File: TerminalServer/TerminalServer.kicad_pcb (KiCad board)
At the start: 2 copper layers, 132 x 72 mm, 87 parts, among them J1 RJ45_LED, J2 RJ45_LED, J3 RJ45_LED, J4 RJ45_LED, J5 RJ45_LED, J6 RJ45_LED, J7 USB_C_Receptacle_USB2.0_14P, U1 PIC32MX795F512L-80x-PT, U2 XR32330EBERTR-F, U3 XR32330EBERTR-F, U4 XR32330EBERTR-F, U5 XR32330EBERTR-F, U6 XR32330EBERTR-F, U7 XR32330EBERTR-F, U8 ESP32-WROOM-32D, U9 TPS82130

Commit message: Progress
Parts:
- added C49: 100nF, Capacitor_SMD:C_0603_1608Metric_Pad1.08x0.95mm_HandSolder, F.Cu at (156.4, 76.5)
- added C50: 100nF, Capacitor_SMD:C_0603_1608Metric_Pad1.08x0.95mm_HandSolder, F.Cu at (81.7, 76.3)
- added C51: 10uF, Capacitor_SMD:C_1206_3216Metric, F.Cu at (78.8, 76.8)
- added J9: Conn_PIC_ICSP_ICD, Connector_PinHeader_2.54mm:PinHeader_1x06_P2.54mm_Vertical, F.Cu at (151.3, 69.5)
- added Y1: SIT8103AI-23-33E-8.00000X, Oscillator:Oscillator_SMD_SiT_PQFN-4Pin_3.2x2.5mm, F.Cu at (152.3, 76.5)
- moved C44 0.75 mm to (150.8, 79.5)
- turned C9 to 180 degrees
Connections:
- U1 pad 63: unconnected-(U1-RC12/OSC1/CLK-Pad63) -> /CLOCK
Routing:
- net VDD: track 355.1 -> 142.9 mm, vias 24 -> 29
- net GND: track 13.4 -> 73.0 mm, vias 7 -> 83
- net /PGM_CLOCK: track 0.00 -> 41.4 mm, vias 0 -> 1
- net /PGM_DATA: track 0.00 -> 38.8 mm, vias 0 -> 1
- net /RESET: track 2.76 -> 30.8 mm, vias 0 -> 1
- net Net-(U3-C1-): track 0.00 -> 21.5 mm
- net Net-(U2-C1-): track 43.0 -> 21.5 mm
- net /CLOCK: track 0.00 -> 5.61 mm
- net /U3RTS: track 36.1 -> 41.5 mm
- net Net-(U3-C1+): track 0.00 -> 4.15 mm
- net Net-(U2-C1+): track 8.30 -> 4.15 mm
- net /U6TXLED: track 108.8 -> 112.5 mm
- net /U6RXLED: track 99.9 -> 102.9 mm
- net /WIFI_INT: track 45.6 -> 43.5 mm
- net /U3RXLED: track 109.0 -> 110.7 mm
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- added copper zone on In2.Cu, net GND
- added copper zone on In1.Cu, net VDD
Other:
- copper layers 2 -> 4

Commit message: Almost complete
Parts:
- removed NT1, NT2: NetTie_2, NetTie:NetTie-2_SMD_Pad2.0mm
- added C52: 100uF/50V, Capacitor_THT:CP_Radial_D8.0mm_P3.50mm, F.Cu at (181.8, 80.6)
- added C53: 220uF/16V, Capacitor_THT:CP_Radial_D6.3mm_P2.50mm, F.Cu at (188.0, 92.2)
- added C54: 100nF, Capacitor_SMD:C_0603_1608Metric_Pad1.08x0.95mm_HandSolder, F.Cu at (163.3, 88.3)
- added J10: Conn_01x06_Pin, Connector_PinHeader_2.54mm:PinHeader_1x06_P2.54mm_Vertical, F.Cu at (84.2, 95.0)
- added J8: Barrel_Jack_Switch, Connector_BarrelJack:BarrelJack_Wuerth_6941xx301002, F.Cu at (171.2, 74.6)
- added LED1: 553-0121F, KiCad:5530121F, F.Cu at (84.4, 131.9)
- added R16: 10k, Resistor_SMD:R_0603_1608Metric_Pad0.98x0.95mm_HandSolder, F.Cu at (83.4, 81.9)
- added R17: 10k, Resistor_SMD:R_0603_1608Metric_Pad0.98x0.95mm_HandSolder, F.Cu at (105.1, 93.8)
- added R18: 10k, Resistor_SMD:R_0603_1608Metric_Pad0.98x0.95mm_HandSolder, F.Cu at (102.0, 93.8)
- added R19: 100R, Resistor_SMD:R_0603_1608Metric_Pad0.98x0.95mm_HandSolder, F.Cu at (82.8, 123.8)
- added R20: 100R, Resistor_SMD:R_0603_1608Metric_Pad0.98x0.95mm_HandSolder, F.Cu at (85.3, 123.8)
- added R21: 2k2, Resistor_SMD:R_0603_1608Metric_Pad0.98x0.95mm_HandSolder, F.Cu at (163.3, 90.2)
- added R22: 2k2, Resistor_SMD:R_0603_1608Metric_Pad0.98x0.95mm_HandSolder, F.Cu at (163.3, 92.0)
- added U10: 24LC16, Package_SO:SOIC-8_3.9x4.9mm_P1.27mm, F.Cu at (156.7, 90.1)
- moved D2 11.6 mm to (178.8, 76.0), turned to 180 degrees
- moved R10 4.41 mm to (136.1, 119.5)
- moved R11 4.41 mm to (124.7, 119.5)
- moved R12 4.41 mm to (102.1, 119.5)
- moved R13 4.41 mm to (90.7, 119.5)
- moved R2 4.41 mm to (187.1, 119.5)
- moved R3 4.41 mm to (175.7, 119.5)
- moved R4 4.41 mm to (170.1, 119.5)
- moved R5 4.41 mm to (158.7, 119.5)
- moved R6 4.41 mm to (119.1, 119.5)
- moved R7 4.41 mm to (107.7, 119.5)
- moved R8 4.41 mm to (153.1, 119.5)
- moved R9 4.41 mm to (141.7, 119.5)
- moved C50 3.05 mm to (84.8, 76.3)
- moved C51 3.05 mm to (81.8, 76.8)
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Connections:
- C46 pad 1: GNDA -> GND
- C47 pad 1: GNDA -> GND
- C48 pad 1: GNDA -> GND
- J1 pad 11: unconnected-(J1-Pad11) -> GND
- J2 pad 11: unconnected-(J2-Pad11) -> GND
- J2 pad 9: unconnected-(J2-Pad9) -> GND
- J3 pad 11: unconnected-(J3-Pad11) -> GND
- J3 pad 9: unconnected-(J3-Pad9) -> GND
- J4 pad 11: unconnected-(J4-Pad11) -> GND
- J4 pad 9: unconnected-(J4-Pad9) -> GND
- J5 pad 11: unconnected-(J5-Pad11) -> GND
- J5 pad 9: unconnected-(J5-Pad9) -> GND
- J6 pad 11: unconnected-(J6-Pad11) -> GND
- J6 pad 9: unconnected-(J6-Pad9) -> GND
- R15 pad 2: GNDA -> GND
- U8 pad 23: unconnected-(U8-IO15-Pad23) -> /ESP_LED
- U8 pad 24: unconnected-(U8-IO2-Pad24) -> Net-(U8-IO2)
- U8 pad 25: unconnected-(U8-IO0-Pad25) -> /ESP_IO0
- U8 pad 3: unconnected-(U8-EN-Pad3) -> /ESP_EN
- U8 pad 34: unconnected-(U8-RXD0/IO3-Pad34) -> /ESP_RX
- U8 pad 35: unconnected-(U8-TXD0/IO1-Pad35) -> /ESP_TX
- U9 pad 3: GNDA -> GND
- U9 pad 9: GNDA -> GND
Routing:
- net /ESP_LED: track 0.00 -> 44.0 mm, vias 0 -> 2
- net /U5RXLED: track 124.2 -> 90.1 mm
- net /U5TXLED: track 133.9 -> 99.8 mm
- net /U4RXLED: track 137.7 -> 103.7 mm
- net /U4TXLED: track 147.5 -> 113.5 mm
- net /U3TXLED: track 120.3 -> 86.4 mm
- net /U2TXLED: track 161.6 -> 127.6 mm
- net /U2RXLED: track 151.6 -> 117.6 mm
- net /U1TXLED: track 175.8 -> 142.4 mm
- net /U1RXLED: track 165.7 -> 132.4 mm
- net /SDA: track 0.00 -> 33.1 mm
- net /SCL: track 0.00 -> 32.7 mm
- net /U3RXLED: track 110.7 -> 81.4 mm
- net /ESP_TX: track 0.00 -> 27.8 mm, vias 0 -> 1
- net /ESP_RX: track 0.00 -> 25.5 mm, vias 0 -> 1
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- removed copper zone on B.Cu, net GNDA
- removed copper zone on F.Cu, net GNDA
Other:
- board size 132 x 72 mm -> 135 x 72 mm

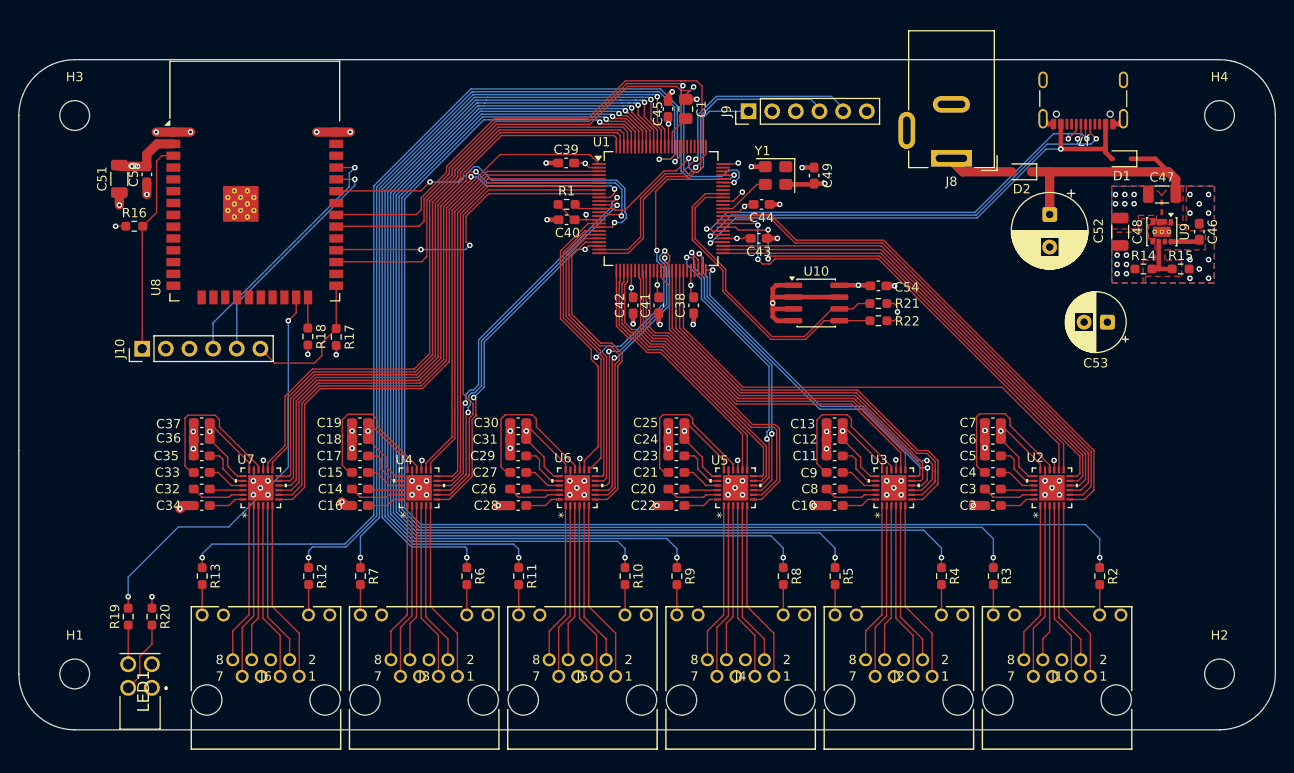
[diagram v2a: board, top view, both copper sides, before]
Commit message: Added Ethernet and more
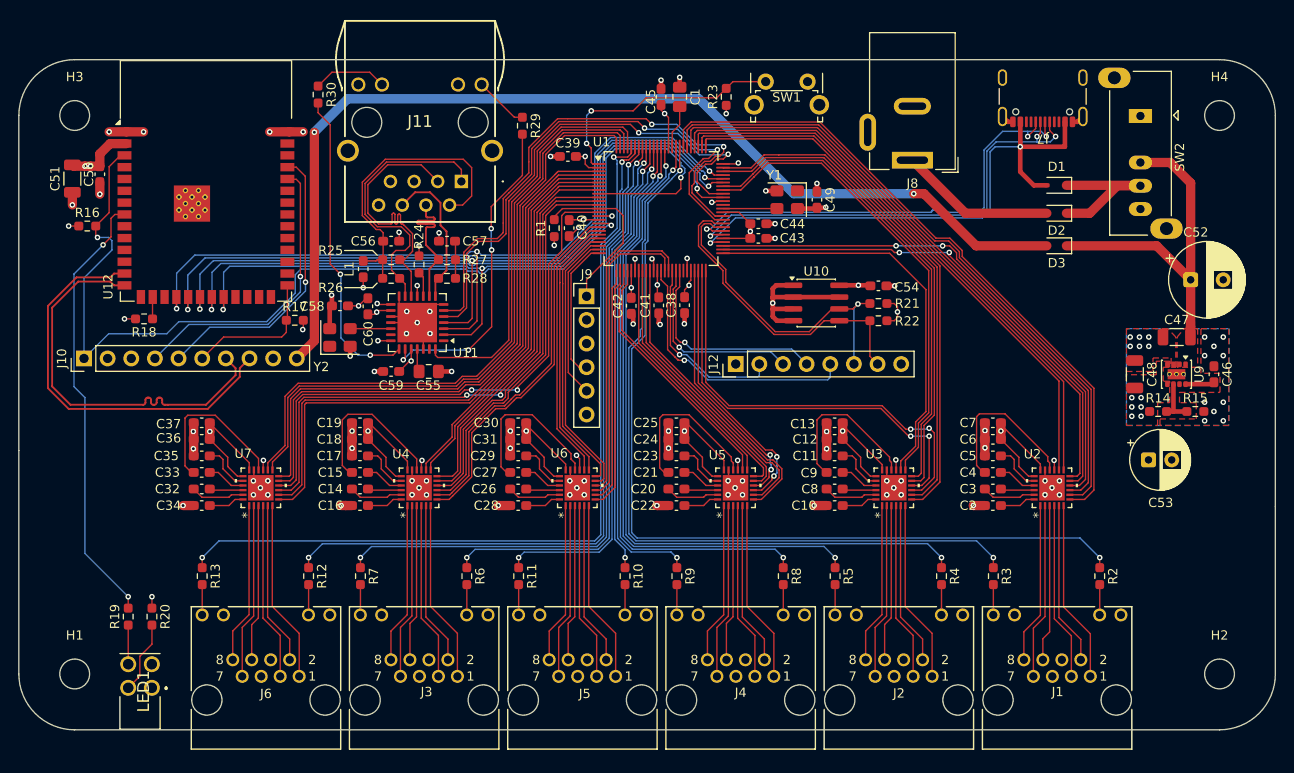
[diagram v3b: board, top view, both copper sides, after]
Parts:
- removed U8: ESP32-WROOM-32D, RF_Module:ESP32-WROOM-32D
- added C55: 10uF, Capacitor_SMD:C_0805_2012Metric_Pad1.18x1.45mm_HandSolder, F.Cu at (115.0, 97.5)
- added C56: 100nF, Capacitor_SMD:C_0603_1608Metric_Pad1.08x0.95mm_HandSolder, F.Cu at (111.0, 83.5)
- added C57: 100nF, Capacitor_SMD:C_0603_1608Metric_Pad1.08x0.95mm_HandSolder, F.Cu at (117.0, 83.5)
- added C58: 100nF, Capacitor_SMD:C_0603_1608Metric_Pad1.08x0.95mm_HandSolder, F.Cu at (105.5, 90.5)
- added C59: 100nF, Capacitor_SMD:C_0603_1608Metric_Pad1.08x0.95mm_HandSolder, F.Cu at (111.0, 97.5)
- added C60: 100nF, Capacitor_SMD:C_0603_1608Metric_Pad1.08x0.95mm_HandSolder, F.Cu at (108.5, 90.5)
- added D3: 1N5819WS, Diode_SMD:D_SOD-323, F.Cu at (182.5, 84.0)
- added J11: SI-60118-F, MagJack:SI60118F, F.Cu at (118.5, 77.1)
- added J12: Conn_01x08_Pin, Connector_PinHeader_2.54mm:PinHeader_1x08_P2.54mm_Vertical, F.Cu at (148.0, 96.7)
- added L1: L_Ferrite, Inductor_SMD:L_0603_1608Metric_Pad1.05x0.95mm_HandSolder, F.Cu at (108.0, 86.5)
- added R23: 10k, Resistor_SMD:R_0603_1608Metric_Pad0.98x0.95mm_HandSolder, F.Cu at (147.0, 68.0)
- added R24: 2k32, Resistor_SMD:R_0603_1608Metric_Pad0.98x0.95mm_HandSolder, F.Cu at (114.0, 86.0)
- added R25: 49R9, Resistor_SMD:R_0603_1608Metric_Pad0.98x0.95mm_HandSolder, F.Cu at (111.0, 85.5)
- added R26: 49R9, Resistor_SMD:R_0603_1608Metric_Pad0.98x0.95mm_HandSolder, F.Cu at (111.0, 87.5)
- added R27: 49R9, Resistor_SMD:R_0603_1608Metric_Pad0.98x0.95mm_HandSolder, F.Cu at (117.0, 85.5)
- added R28: 49R9, Resistor_SMD:R_0603_1608Metric_Pad0.98x0.95mm_HandSolder, F.Cu at (117.0, 87.5)
- added R29: 100R, Resistor_SMD:R_0603_1608Metric_Pad0.98x0.95mm_HandSolder, F.Cu at (125.1, 71.1)
- added R30: 100R, Resistor_SMD:R_0603_1608Metric_Pad0.98x0.95mm_HandSolder, F.Cu at (103.2, 67.8)
- added SW1: SW_Push, Button_Switch_THT:SW_Tactile_SPST_Angled_PTS645Vx31-2LFS, F.Cu at (151.2, 66.4)
- added SW2: SW_SPDT, Button_Switch_THT:SW_Slide_SP3T_Straight_CK_OS103012MU1QP1, F.Cu at (191.5, 70.0)
- added U11: ENC28J60x-ML, Package_DFN_QFN:QFN-28-1EP_6x6mm_P0.65mm_EP4.25x4.25mm, F.Cu at (113.8, 92.2)
- added U12: ESP32-S3-WROOM-1, RF_Module:ESP32-S3-WROOM-1, F.Cu at (91.1, 77.0)
- added Y2: ASEMB-25.000MHZ-LC-T, Oscillator:Oscillator_SMD_SiT_PQFN-4Pin_3.2x2.5mm, F.Cu at (105.5, 93.8)
- J10: footprint Connector_PinHeader_2.54mm:PinHeader_1x06_P2.54mm_Vertical -> Connector_PinHeader_2.54mm:PinHeader_1x10_P2.54mm_Vertical
- LED1: footprint KiCad:5530121F -> LEDS:5530121F
- Y1: value SIT8103AI-23-33E-8.00000X -> ASEMB-8.000MHZ-LC-T
- moved J9 26.4 mm to (132.0, 89.4), turned to 0 degrees
- moved R18 17.7 mm to (84.5, 91.8), turned to 180 degrees
- moved C52 16.7 mm to (196.9, 87.7), turned to 0 degrees
- moved C53 15.4 mm to (192.4, 107.0), turned to 0 degrees
- moved C46 15.4 mm to (199.4, 97.8)
- moved C47 15.4 mm to (195.4, 93.8)
- moved C48 15.4 mm to (190.9, 97.8)
- moved R14 15.4 mm to (193.4, 101.8)
- moved R15 15.4 mm to (197.4, 101.8)
- moved U9 15.4 mm to (195.4, 97.8)
- moved D1 7.56 mm to (182.5, 77.5)
- moved J10 6.34 mm to (78.0, 96.1)
- moved D2 5.82 mm to (182.5, 80.5)
- moved R16 5.05 mm to (78.3, 81.9)
- moved C51 5.05 mm to (76.8, 76.8)
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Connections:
- net /USB_DM renamed /USBD_M
- net /USB_DP renamed /USBD_P
- D1 pad 1: VCC -> /SWIN
- D2 pad 1: VCC -> /SWIN
- J10 pad 4: /ESP_TX -> /ESP_RX
- J10 pad 5: /ESP_RX -> /ESP_TX
- U1 pad 1: /U6DTR -> /FRES
- U1 pad 17: /U5SHTDN -> /ESP_EN
- U1 pad 18: /WIFI_INT -> /U3DTR
- U1 pad 19: /U5CTS -> /U3RTS
- U1 pad 20: /U5DSR -> /U5SHTDN
- U1 pad 21: /U5DTR -> /U5STATUS
- U1 pad 22: /U5RTS -> /U5CTS
- U1 pad 23: /U3RTS -> /U5DSR
- U1 pad 26: /U4SHTDN -> /U5DTR
- U1 pad 27: /U4STATUS -> /U5RTS
- U1 pad 28: /U4CTS -> /U4SHTDN
- U1 pad 29: /U4DSR -> /U4STATUS
- U1 pad 3: /U6RTS -> /U6DTR
- U1 pad 32: /U4DTR -> /U4CTS
- U1 pad 33: /U4RTS -> /U4DSR
- U1 pad 34: /U2SHTDN -> /U4DTR
- U1 pad 35: /U2STATUS -> /U4RTS
- U1 pad 38: /U2CTS -> /GPIO3
- U1 pad 4: /U3SHTDN -> /U6RTS
- U1 pad 41: /U2DSR -> /GPIO0
- U1 pad 42: /U2DTR -> /GPIO1
- U1 pad 43: /U2RTS -> /GPIO2
- U1 pad 44: /U1SHTDN -> unconnected-(U1-RB15-Pad44)
- U1 pad 5: /U3STATUS -> /U3SHTDN
- U1 pad 51: /U1DSR -> /U2SHTDN
- U1 pad 58: /U1CTS -> /SCL
- U1 pad 59: /U1STATUS -> /SDA
- U1 pad 6: /U3CTS -> /U3STATUS
- U1 pad 60: /U1DTR -> /ENC_SEL
- U1 pad 61: /U1RTS -> /ENC_RESET
- U1 pad 66: /SCL -> /ESP_INT
- U1 pad 67: /SDA -> /ENC_INT
- U1 pad 68: unconnected-(U1-RD8-Pad68) -> /U2STATUS
- U1 pad 69: unconnected-(U1-RD9-Pad69) -> /U2CTS
- U1 pad 7: /U3DSR -> /U3CTS
- U1 pad 70: /SCK -> /SPI_SCK
- U1 pad 71: unconnected-(U1-RD11-Pad71) -> /ESP_SEL
- U1 pad 72: /SDO -> /SPI_MOSI
- U1 pad 73: unconnected-(U1-RC13/SOSCI-Pad73) -> /U2DSR
- U1 pad 74: unconnected-(U1-RC14/SOSCO-Pad74) -> /U2DTR
- U1 pad 76: /U5STATUS -> /U2RTS
- U1 pad 77: /WIFI_SEL -> /U1SHTDN
- U1 pad 78: unconnected-(U1-RD3-Pad78) -> /U1STATUS
- U1 pad 79: unconnected-(U1-RD12-Pad79) -> /U1CTS
- U1 pad 8: /U3DTR -> /U3DSR
- U1 pad 80: unconnected-(U1-RD13-Pad80) -> /U1DSR
- U1 pad 81: unconnected-(U1-RD4-Pad81) -> /U1DTR
- U1 pad 82: unconnected-(U1-RD5-Pad82) -> /U1RTS
- U1 pad 83: /U6RXLED -> /U1TXLED
- U1 pad 84: /U6TXLED -> /U1RXLED
- U1 pad 87: /U3RXLED -> /U2TXLED
- U1 pad 88: /U3TXLED -> /U2RXLED
- U1 pad 89: /U5RXLED -> /U4TXLED
- U1 pad 9: /SDI -> /SPI_MISO
- U1 pad 90: /U5TXLED -> /U4RXLED
- U1 pad 91: /U4RXLED -> /U5TXLED
- U1 pad 92: /U4TXLED -> /U5RXLED
- U1 pad 93: /U2RXLED -> /U3TXLED
- U1 pad 94: /U2TXLED -> /U3RXLED
- U1 pad 95: /U1RXLED -> /U6TXLED
- U1 pad 96: /U1TXLED -> /U6RXLED
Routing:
- net Net-(D3-A): track 0.00 -> 111.8 mm, vias 0 -> 2
- net /SPI_MISO: track 0.00 -> 87.8 mm, vias 0 -> 3
- net /SPI_MOSI: track 0.00 -> 87.3 mm, vias 0 -> 3
- net /SPI_SCK: track 0.00 -> 83.2 mm, vias 0 -> 3
- net /ESP_SEL: track 0.00 -> 74.9 mm, vias 0 -> 2
- net /ESP_INT: track 0.00 -> 73.6 mm, vias 0 -> 2
- net /SCK: track 68.9 -> 0.00 mm, vias 2 -> 0
- net /ESP_EN: track 22.8 -> 91.5 mm, vias 0 -> 2
- net /ENC_INT: track 0.00 -> 62.8 mm, vias 0 -> 2
- net /SDO: track 62.2 -> 0.00 mm, vias 2 -> 0
- net /ENC_RESET: track 0.00 -> 58.5 mm, vias 0 -> 2
- net /ENC_SEL: track 0.00 -> 57.6 mm, vias 0 -> 2
- net /WIFI_SEL: track 53.1 -> 0.00 mm
- net /U5TXLED: track 99.8 -> 47.3 mm
- net /U4RXLED: track 103.7 -> 52.0 mm
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
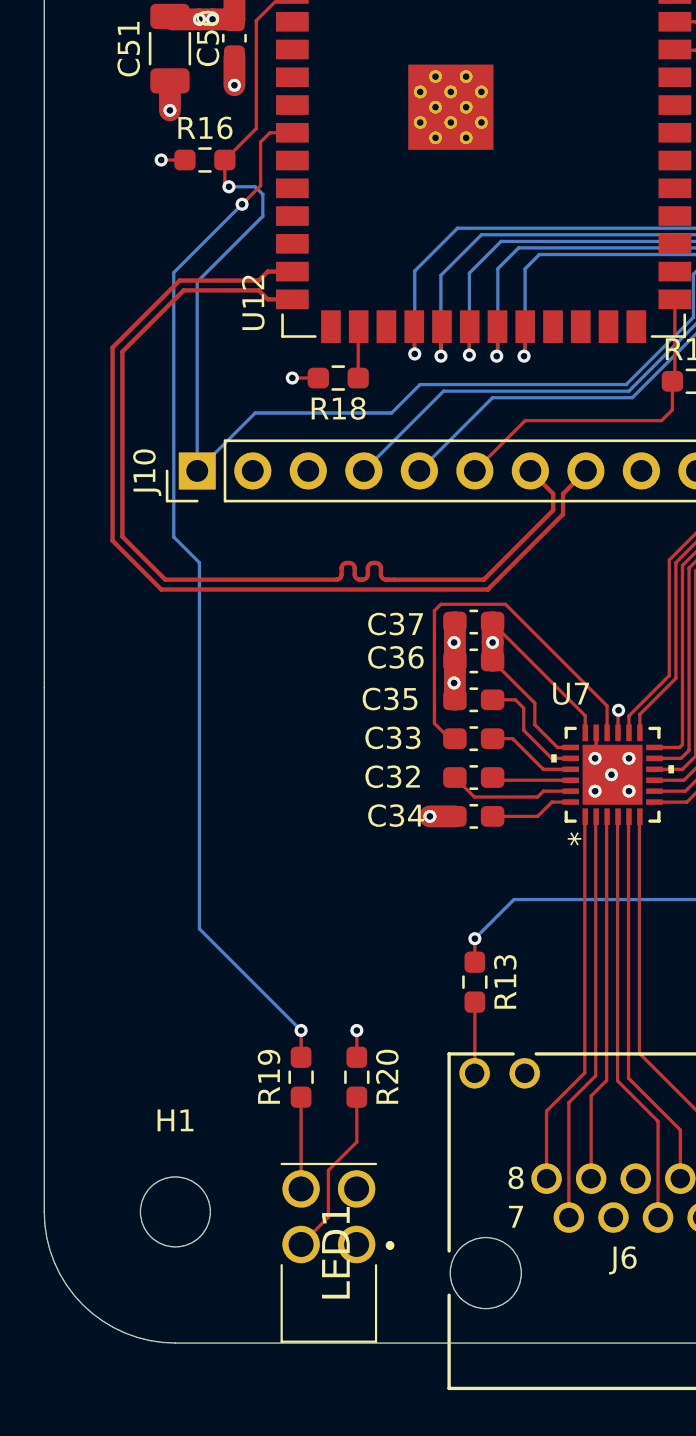
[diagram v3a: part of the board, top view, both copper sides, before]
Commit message: Added 4-led module
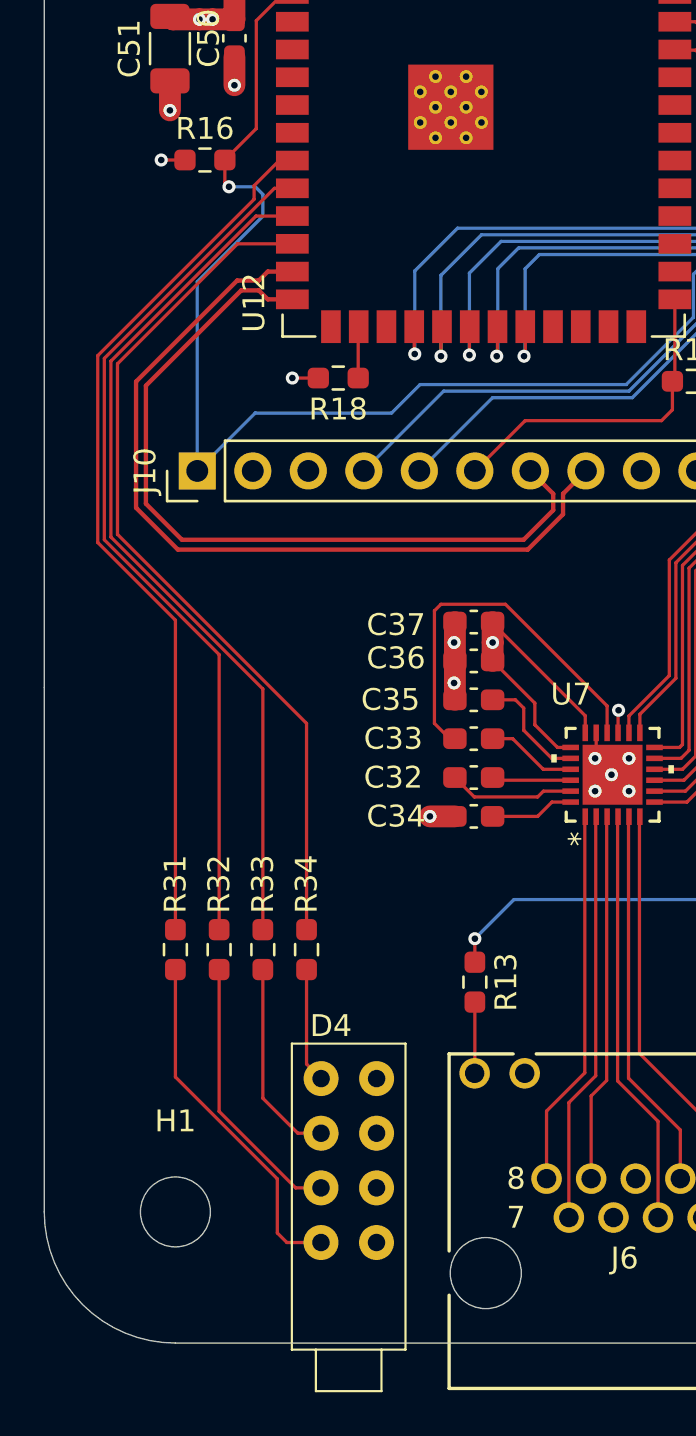
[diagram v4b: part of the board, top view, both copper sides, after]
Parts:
- removed LED1: 553-0121F, LEDS:5530121F
- removed R19, R20: 100R, Resistor_SMD:R_0603_1608Metric_Pad0.98x0.95mm_HandSolder
- added D4: XL-DZ234SYGD-4, XINGLIGHT:XL-DZ234SYGD-4, F.Cu at (84.9, 129.3)
- added R31: 100R, Resistor_SMD:R_0603_1608Metric_Pad0.98x0.95mm_HandSolder, F.Cu at (77.0, 118.0)
- added R32: 100R, Resistor_SMD:R_0603_1608Metric_Pad0.98x0.95mm_HandSolder, F.Cu at (79.0, 118.0)
- added R33: 100R, Resistor_SMD:R_0603_1608Metric_Pad0.98x0.95mm_HandSolder, F.Cu at (81.0, 118.0)
- added R34: 100R, Resistor_SMD:R_0603_1608Metric_Pad0.98x0.95mm_HandSolder, F.Cu at (83.0, 118.0)
- J10: value Conn_01x06_Pin -> Conn_01x10_Pin
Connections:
- U12 pad 10: unconnected-(U12-IO17-Pad10) -> /LED2
- U12 pad 11: unconnected-(U12-IO18-Pad11) -> /LED3
- U12 pad 12: unconnected-(U12-IO8-Pad12) -> /LED4
- U12 pad 9: unconnected-(U12-IO16-Pad9) -> /LED1
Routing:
- net /ESP_LED: track 47.6 -> 0.00 mm, vias 2 -> 0
- net /LED1: track 0.00 -> 40.7 mm
- net /LED2: track 0.00 -> 40.1 mm
- net /LED3: track 0.00 -> 39.9 mm
- net /LED4: track 0.00 -> 39.7 mm
- net Net-(D4-LED_A1): track 0.00 -> 16.2 mm
- net Net-(D4-LED_A2): track 0.00 -> 12.6 mm
- net Net-(D4-LED_A3): track 0.00 -> 9.21 mm
- net Net-(LED1-A_1): track 7.80 -> 0.00 mm
- net /ESP_USB_P: track 43.8 -> 36.2 mm
- net /ESP_USB_N: track 43.9 -> 38.4 mm
- net Net-(D4-LED_A4): track 0.00 -> 5.26 mm
- net Net-(LED1-A_2): track 4.20 -> 0.00 mm
- net VDD: track 159.4 -> 158.2 mm, vias 42 -> 41
